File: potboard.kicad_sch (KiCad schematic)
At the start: 18 parts, among them J2 BH254

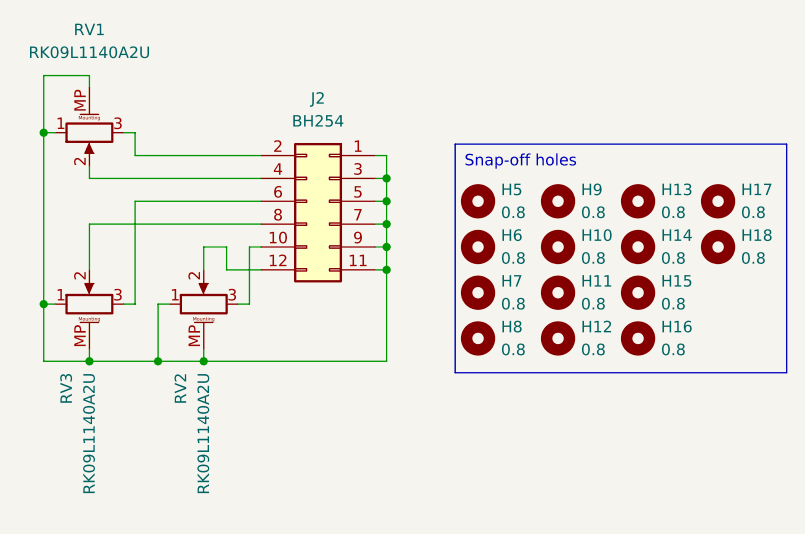
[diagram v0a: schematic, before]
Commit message: Pot board made smaller using MicroMatch connectors. Snap-off holes tidied up, and gap increased to 2mm for compatibility with some PCB manufacturer's design rules.
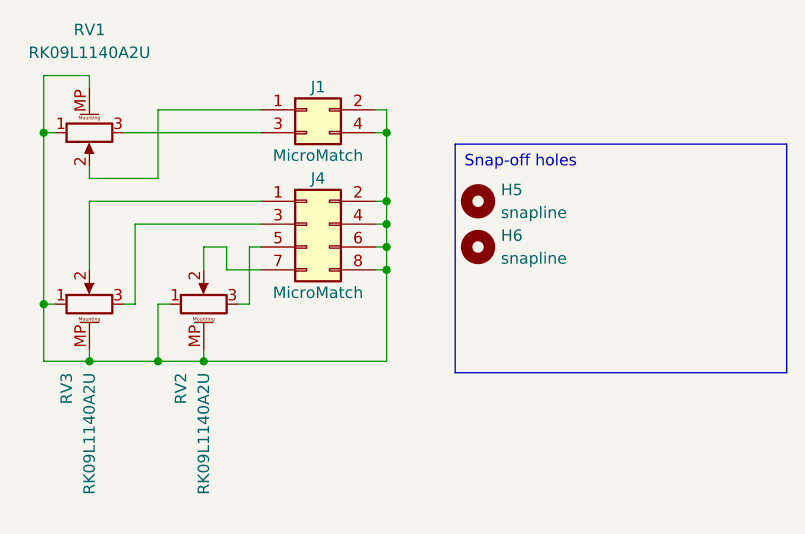
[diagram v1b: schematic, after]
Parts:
- removed H10, H11, H12, H13, H14, H15, H16, H17, H18, H7, H8, H9: 0.8, HR_Parts:HOLE_0.8, symbol Mechanical:MountingHole
- removed J2: BH254, Connector_IDC:IDC-Header_2x06_P2.54mm_Vertical, symbol Connector_Generic:Conn_02x06_Odd_Even
- added J1: MicroMatch, Connector_TE-Connectivity:TE_Micro-MaTch_215079-4_2x02_P1.27mm_Vertical, symbol Connector_Generic:Conn_02x02_Odd_Even
- added J4: MicroMatch, Connector_TE-Connectivity:TE_Micro-MaTch_215079-8_2x04_P1.27mm_Vertical, symbol Connector_Generic:Conn_02x04_Odd_Even
- H5, H6: value 0.8 -> snapline; footprint HR_Parts:HOLE_0.8 -> HR_Parts:SNAPOFF_5x0.6_P1.2
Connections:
- net at RV1.1, RV1.MP (MountPin), RV2.1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: now also J1.2 (Pin_2), J1.4 (Pin_4), J4.2 (Pin_2), J4.4 (Pin_4), J4.6 (Pin_6), J4.8 (Pin_8)
- net at RV3.2: now also J4.1 (Pin_1)
- net at RV3.3: now also J4.3 (Pin_3)
- net at RV1.2: now also J1.1 (Pin_1)
- net at RV1.3: now also J1.3 (Pin_3)
- net at RV2.3: now also J4.5 (Pin_5)
- net at RV2.2: now also J4.7 (Pin_7)
